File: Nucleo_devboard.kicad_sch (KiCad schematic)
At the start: 1 part, among them J2 Conn_ARM_SWD_TagConnect_TC203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

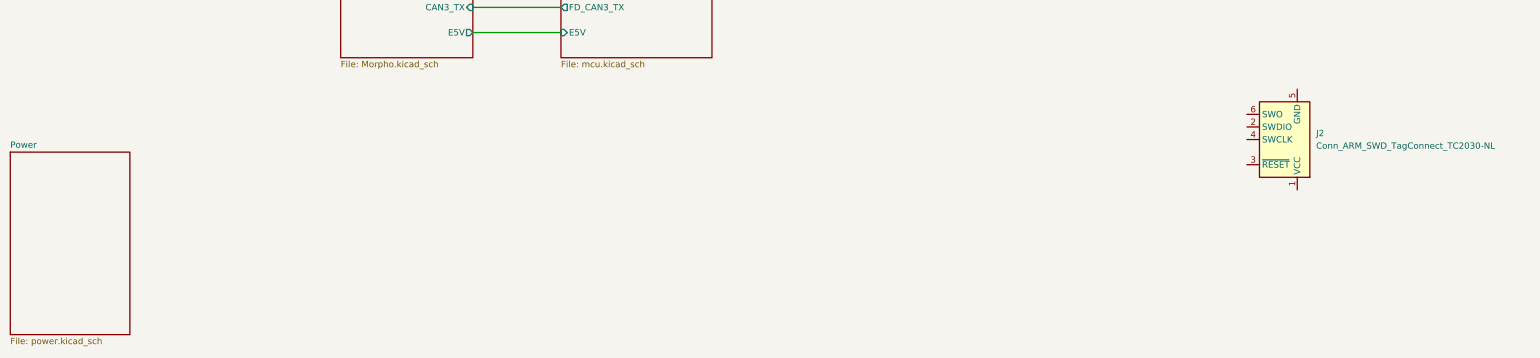
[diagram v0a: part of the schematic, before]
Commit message: Added finishing thouches to brake sense pcb Finished main schematic layout and added chosen component footprints Placed components in layout and started tracing
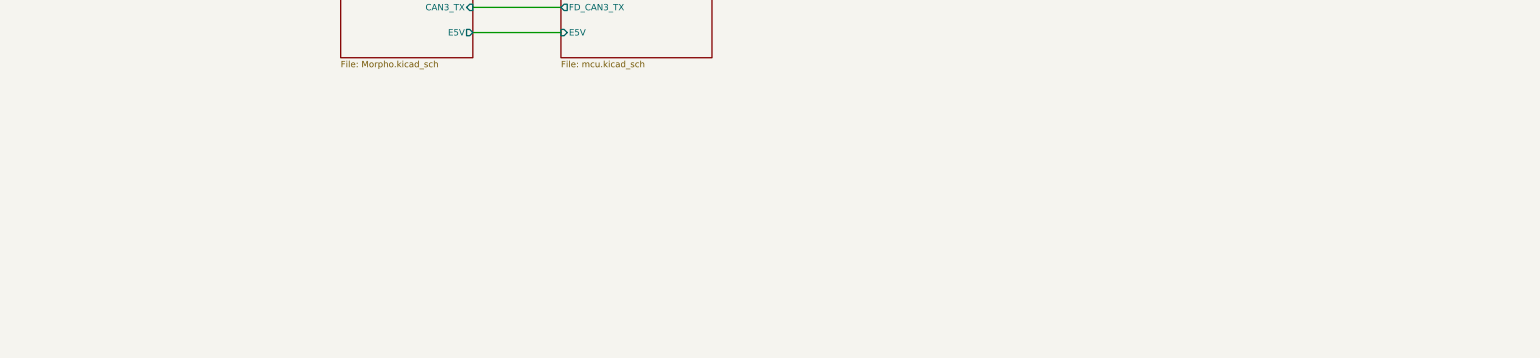
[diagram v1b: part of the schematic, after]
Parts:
- removed J2: Conn_ARM_SWD_TagConnect_TC2030-NL, Connector:Tag-Connect_TC2030-IDC-NL_2x03_P1.27mm_Vertical, symbol Connector:Conn_ARM_SWD_TagConnect_TC2030-NL
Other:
- removed sheet Power
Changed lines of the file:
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@@
-		)
-	)
-	(symbol
-		(lib_id "Connector:Conn_ARM_SWD_TagConnect_TC2030-NL")
-		(at 273.05 151.13 180)
-		(unit 1)
-		(body_style 1)
-		(exclude_from_sim no)
-		(in_bom no)
-		(on_board yes)
-		(in_pos_files yes)
-		(dnp no)
-		(fields_autoplaced yes)
-		(property "Reference" "J2"
-			(at 279.4 149.8599 0)
-			(show_name no)
-			(do_not_autoplace no)
-			(effects
-				(font
-					(size 1.27 1.27)
-				)
-				(justify right)
-			)
-		)
-		(property "Value" "Conn_ARM_SWD_TagConnect_TC2030-NL"
-			(at 279.4 152.3999 0)
-			(show_name no)
-			(do_not_autoplace no)
-			(effects
-				(font
-					(size 1.27 1.27)
-				)
-				(justify right)
-			)
-		)
-		(property "Footprint" "Connector:Tag-Connect_TC2030-IDC-NL_2x03_P1.27mm_Vertical"
-			(at 273.05 133.35 0)
-			(hide yes)
-			(show_name no)
-			(do_not_autoplace no)
-			(effects
-				(font
-					(size 1.27 1.27)
-				)
-			)
-		)
-		(property "Datasheet" "https://www.tag-connect.com/wp-content/uploads/bsk-pdf-manager/TC2030-CTX_1.pdf"
-			(at 273.05 135.89 0)
-			(hide yes)
-			(show_name no)
-			(do_not_autoplace no)
-			(effects
-				(font
-					(size 1.27 1.27)
-				)
-			)
-		)
-		(property "Description" "Tag-Connect ARM Cortex SWD JTAG connector, 6 pin, no legs"
-			(at 273.05 151.13 0)
-			(hide yes)
-			(show_name no)
-			(do_not_autoplace no)
-			(effects
-				(font
-					(size 1.27 1.27)
-				)
-			)
-		)
-		(pin "3"
-		)
-		(pin "1"
-		)
-		(pin "2"
-		)
-		(pin "5"
-		)
-		(pin "6"
-		)
-		(pin "4"
-		)
-		(instances
-			(project "kiCad_test"
-				(path "/4250c3cc-f8c5-441a-9e80-e89bb6ada756"
-					(reference "J2")
-					(unit 1)
-				)
-			)
 		)
 	)
@@
 		)
 		(instances
-			(project "kiCad_test"
+			(project "Nucleo_devboard"
 				(path "/4250c3cc-f8c5-441a-9e80-e89bb6ada756"
 					(page "2")
@@
 		)
 		(instances
-			(project "kiCad_test"
+			(project "Nucleo_devboard"
 				(path "/4250c3cc-f8c5-441a-9e80-e89bb6ada756"
 					(page "5")
 				)
 			)
-		)
-	)
-	(sheet
-		(at 15.875 153.67)
-		(size 24.13 36.83)
-		(exclude_from_sim no)
-		(in_bom yes)
-		(on_board yes)
-		(dnp no)
-		(fields_autoplaced yes)
-		(stroke
-			(width 0.1524)
-			(type solid)
-		)
-		(fill
-			(color 0 0 0 0)
-		)
-		(property "Sheetname" "Power"
-			(at 15.875 152.9584 0)
-			(show_name no)
-			(do_not_autoplace no)
-			(effects
-				(font
-					(size 1.27 1.27)
-				)
-				(justify left bottom)
-			)
-		)
-		(property "Sheetfile" "power.kicad_sch"
-			(at 15.875 191.0846 0)
-			(show_name no)
-			(do_not_autoplace no)
-			(effects
-				(font
-					(size 1.27 1.27)
-				)
-				(justify left top)
-			)
-		)
-		(instances
-			(project "kiCad_test"
-				(path "/4250c3cc-f8c5-441a-9e80-e89bb6ada756"
-					(page "4")
-				)
-			)

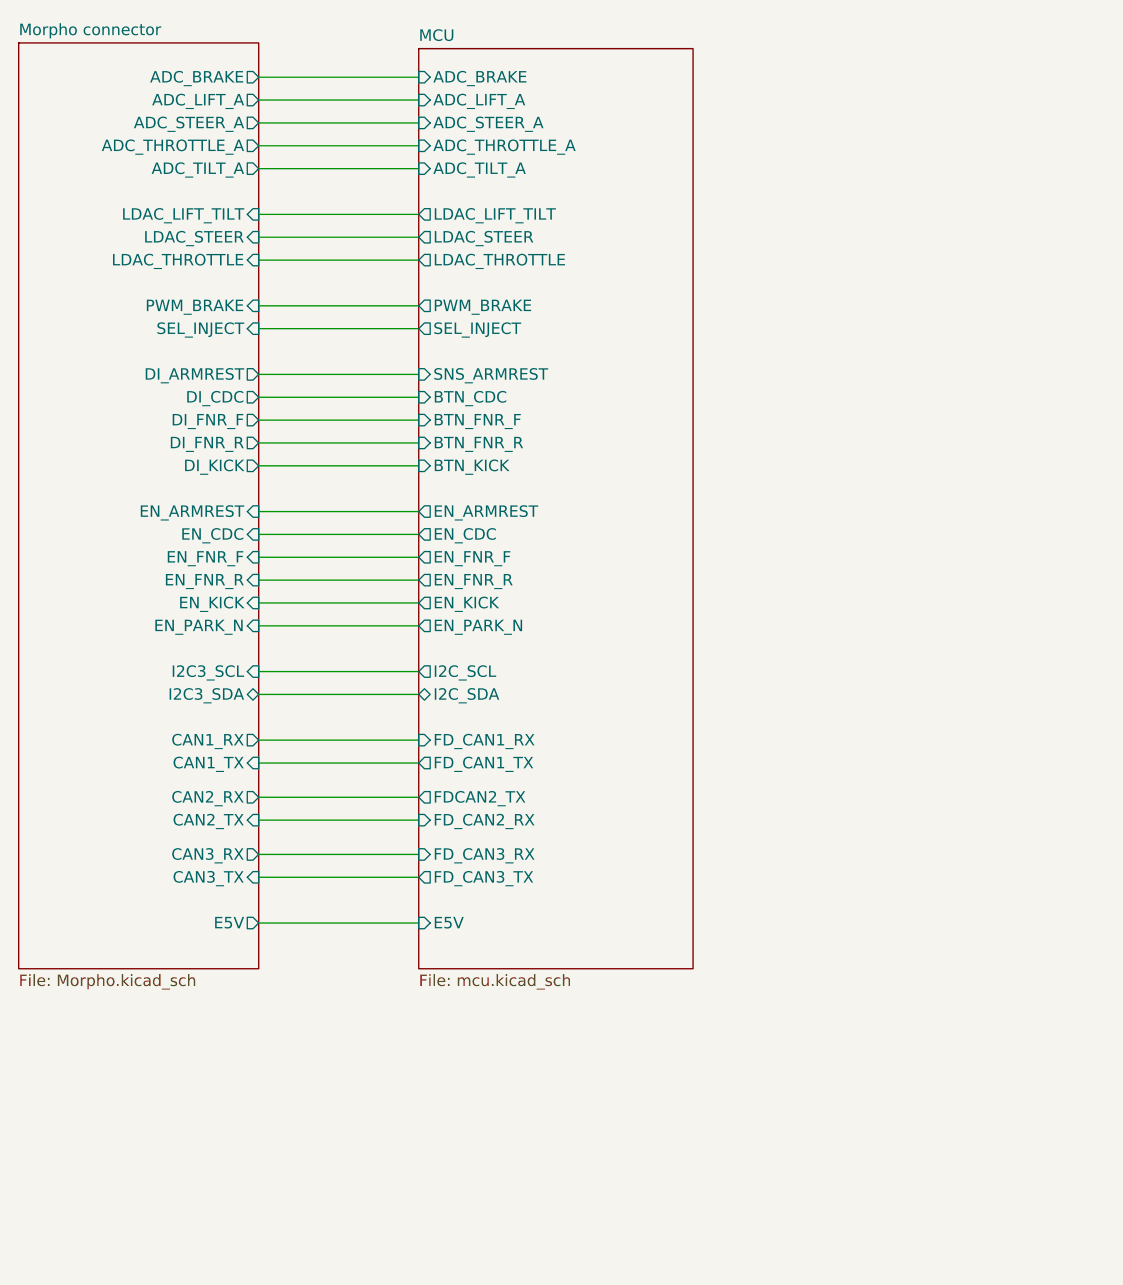
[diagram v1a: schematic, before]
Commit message: added rev04_mcu1/2.h revised brake sense board Added logic for 2 MCUs on nucleo board
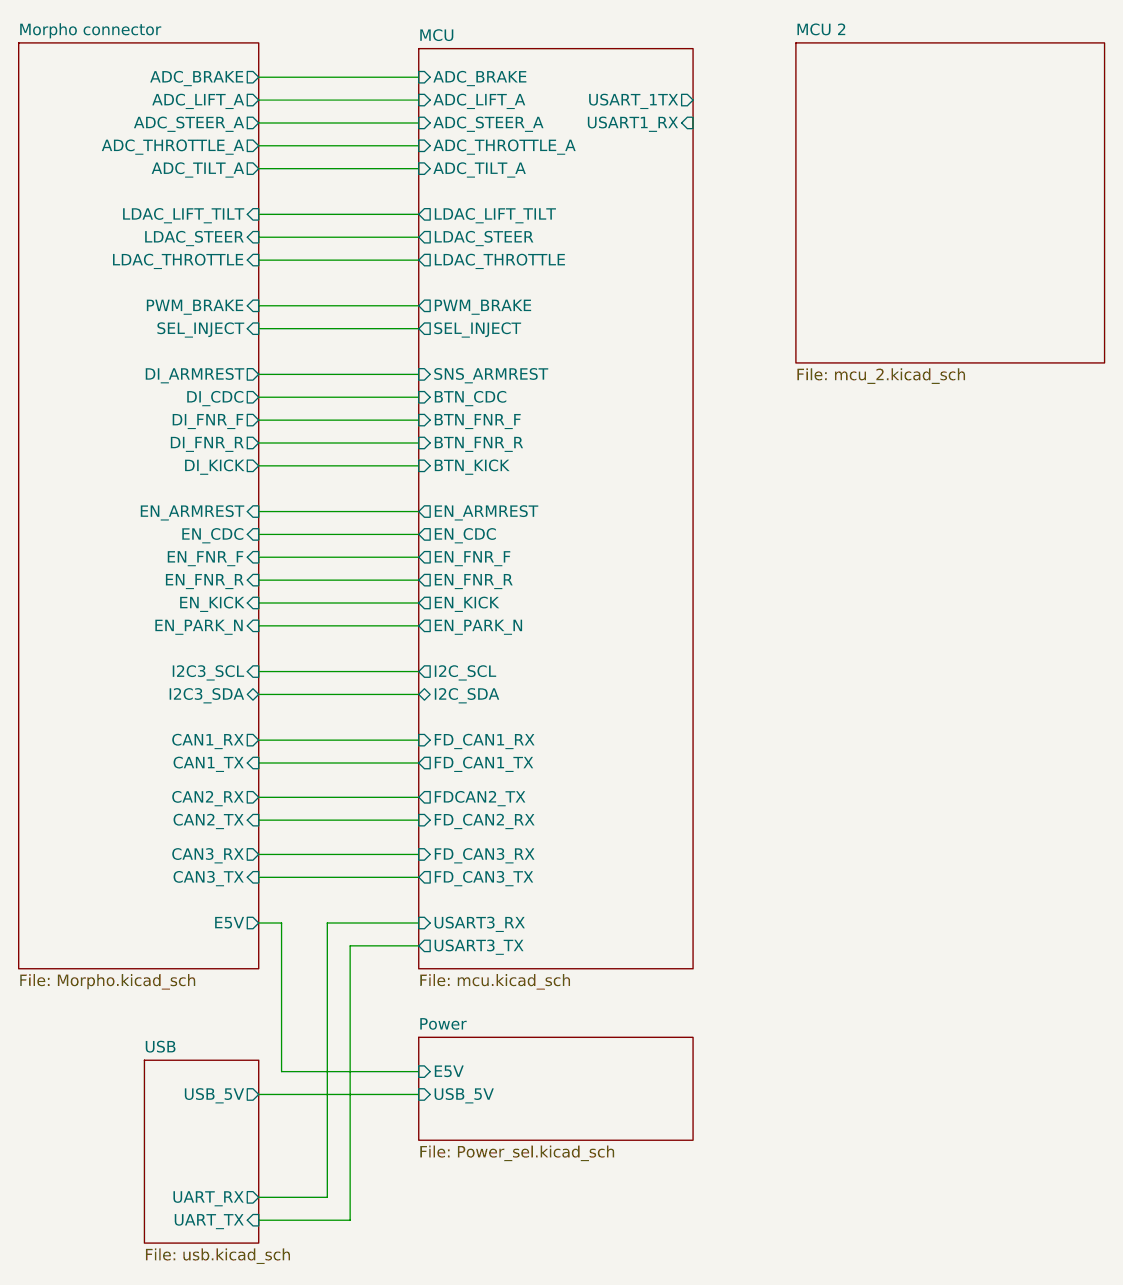
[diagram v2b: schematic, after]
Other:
- added sheet MCU 2 (mcu_2.kicad_sch)
- added sheet Power (Power_sel.kicad_sch)
- added sheet USB (usb.kicad_sch)
- sheet MCU ports: added USART1_RX, USART3_RX, USART3_TX, USART_1TX; removed E5V

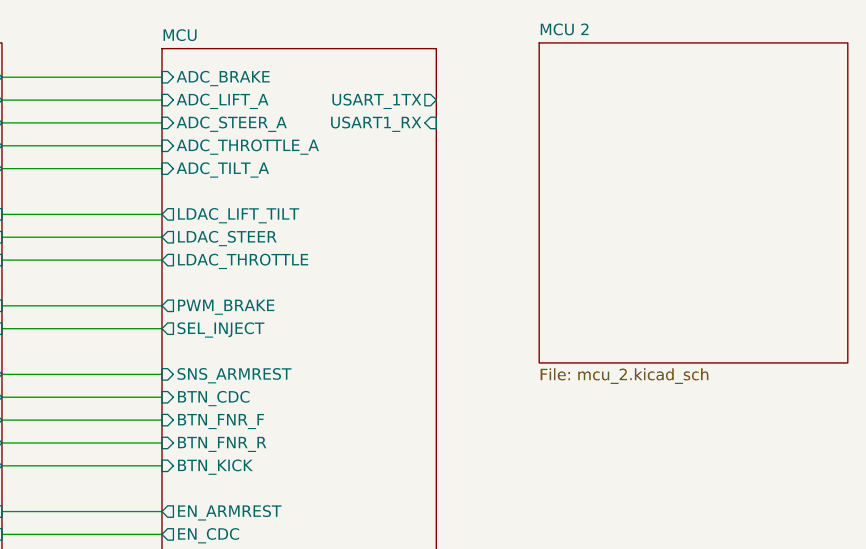
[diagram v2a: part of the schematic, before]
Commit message: Generated scaffold for mcu2 finished brake sense rev2 finished adding second chip to nucleo devboard
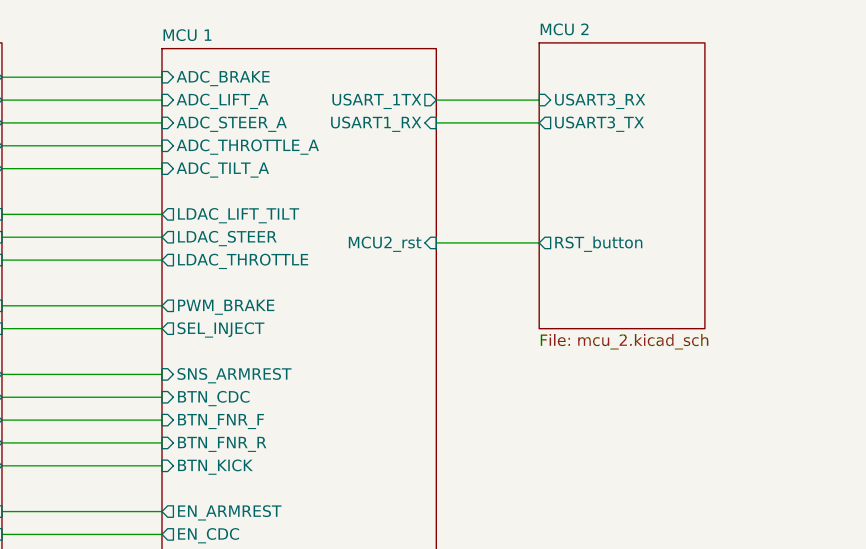
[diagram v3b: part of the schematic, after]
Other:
- sheet MCU renamed MCU 1
- sheet MCU 1 ports: added MCU2_rst; removed none
- sheet MCU 2 ports: added RST_button, USART3_RX, USART3_TX; removed none
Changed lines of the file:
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@@
+	(wire
+		(pts
+			(xy 157.48 53.975) (xy 168.91 53.975)
+		)
+		(stroke
+			(width 0)
+			(type default)
+		)
+	)
+	(wire
+		(pts
+			(xy 157.48 38.1) (xy 168.91 38.1)
+		)
+		(stroke
+			(width 0)
+			(type default)
+		)
+	)
 	(wire
 		(pts
@@
 		(pts
 			(xy 111.76 146.05) (xy 127 146.05)
+		)
+		(stroke
+			(width 0)
+			(type default)
+		)
+	)
+	(wire
+		(pts
+			(xy 157.48 40.64) (xy 168.91 40.64)
 		)
 		(stroke
@@
 			(color 0 0 0 0)
 		)
-		(property "Sheetname" "MCU"
+		(property "Sheetname" "MCU 1"
 			(at 127 31.6734 0)
 			(show_name no)
@@
 		(pin "USART_1TX" output
 			(at 157.48 38.1 0)
+			(effects
+				(font
+					(size 1.27 1.27)
+				)
+				(justify right)
+			)
+		)
+		(pin "MCU2_rst" input
+			(at 157.48 53.975 0)
 			(effects
 				(font
@@
 	(sheet
 		(at 168.91 31.75)
-		(size 34.29 35.56)
+		(size 18.415 31.75)
 		(exclude_from_sim no)
 		(in_bom yes)
@@
 		)
 		(property "Sheetfile" "mcu_2.kicad_sch"
-			(at 168.91 67.8946 0)
+			(at 168.91 64.0846 0)
 			(show_name no)
 			(do_not_autoplace no)
@@
 			)
 		)
+		(pin "RST_button" output
+			(at 168.91 53.975 180)
+			(effects
+				(font
+					(size 1.27 1.27)
+				)
+				(justify left)
+			)
+		)
+		(pin "USART3_RX" input
+			(at 168.91 38.1 180)
+			(effects
+				(font
+					(size 1.27 1.27)
+				)
+				(justify left)
+			)
+		)
+		(pin "USART3_TX" output
+			(at 168.91 40.64 180)
+			(effects
+				(font
+					(size 1.27 1.27)
+				)
+				(justify left)
+			)
+		)
